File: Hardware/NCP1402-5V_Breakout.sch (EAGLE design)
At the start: 11 parts, among them U1 NCP1402

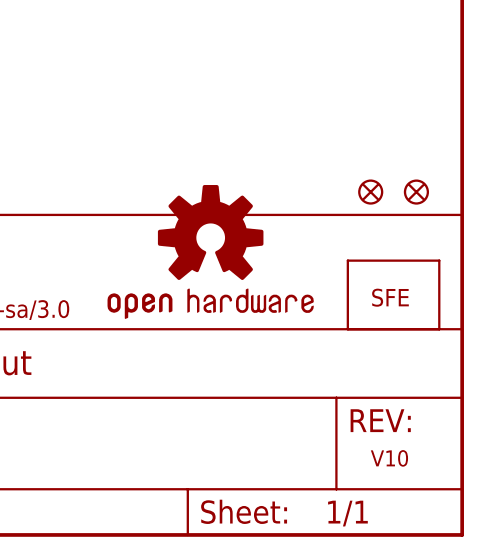
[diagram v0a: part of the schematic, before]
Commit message: changed fiducials to regular from micro
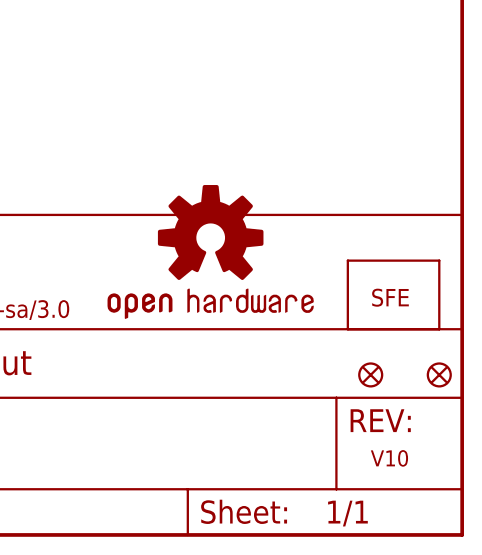
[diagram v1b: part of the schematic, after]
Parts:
- removed JP3, JP4: FIDUCIALUFIDUCIAL, SparkFun:FIDUCIALUFIDUCIAL
- added FID1, FID2: FIDUCIAL1X2, SparkFun-Aesthetics:FIDUCIAL1X2
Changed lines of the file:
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@@
 <?xml version="1.0" encoding="utf-8"?>
 <!DOCTYPE eagle SYSTEM "eagle.dtd">
-<eagle version="6.4">
+<eagle version="6.5.0">
 <drawing>
 <settings>
@@
 <part name="JP2" library="SparkFun" deviceset="LOGO-SFE" device="SK"/>
 <part name="U$1" library="SparkFun" deviceset="OSHW-LOGO" device="S"/>
-<part name="JP3" library="SparkFun" deviceset="FIDUCIAL" device="UFIDUCIAL"/>
-<part name="JP4" library="SparkFun" deviceset="FIDUCIAL" device="UFIDUCIAL"/>
+<part name="FID1" library="SparkFun-Aesthetics" deviceset="FIDUCIAL" device="1X2"/>
+<part name="FID2" library="SparkFun-Aesthetics" deviceset="FIDUCIAL" device="1X2"/>
 </parts>
 <sheets>
@@
 <instance part="JP2" gate="G$1" x="238.76" y="25.4"/>
 <instance part="U$1" gate="G$1" x="220.98" y="33.02"/>
-<instance part="JP3" gate="G$1" x="243.84" y="38.1"/>
-<instance part="JP4" gate="G$1" x="238.76" y="38.1"/>
+<instance part="FID1" gate="G$1" x="238.76" y="17.78"/>
+<instance part="FID2" gate="G$1" x="246.38" y="17.78"/>
 </instances>
 <busses>
